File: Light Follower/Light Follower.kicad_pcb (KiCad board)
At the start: 2 copper layers, 144.8 x 86.5 mm, 14 parts, among them P1 Digital, P2 Analog, P3 CONN_01X01, P4 CONN_01X01, P5 CONN_01X01, P6 CONN_01X01

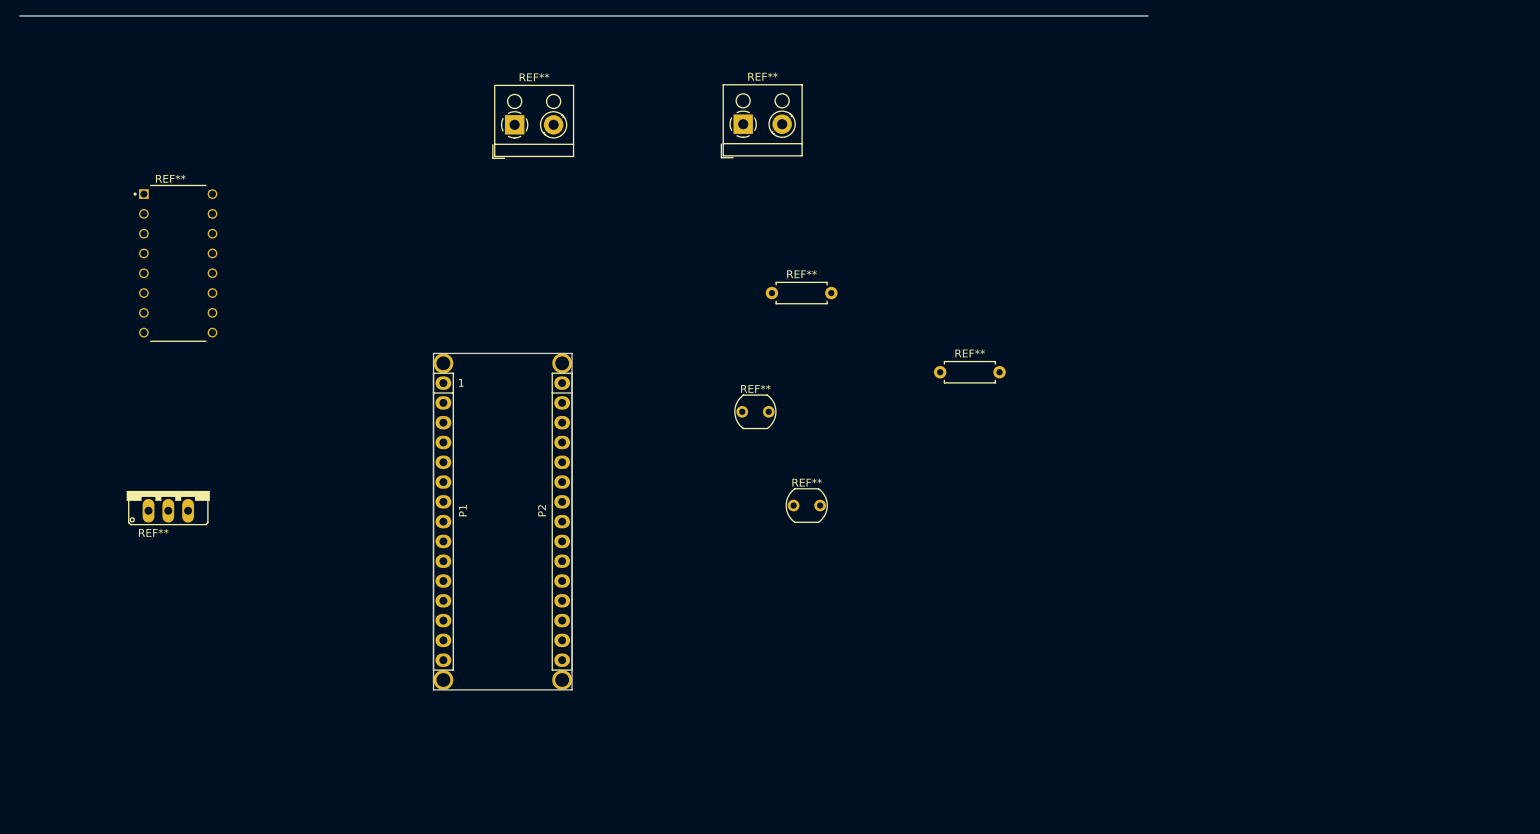
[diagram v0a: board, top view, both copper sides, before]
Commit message: Added PCB Design and LDR Modules
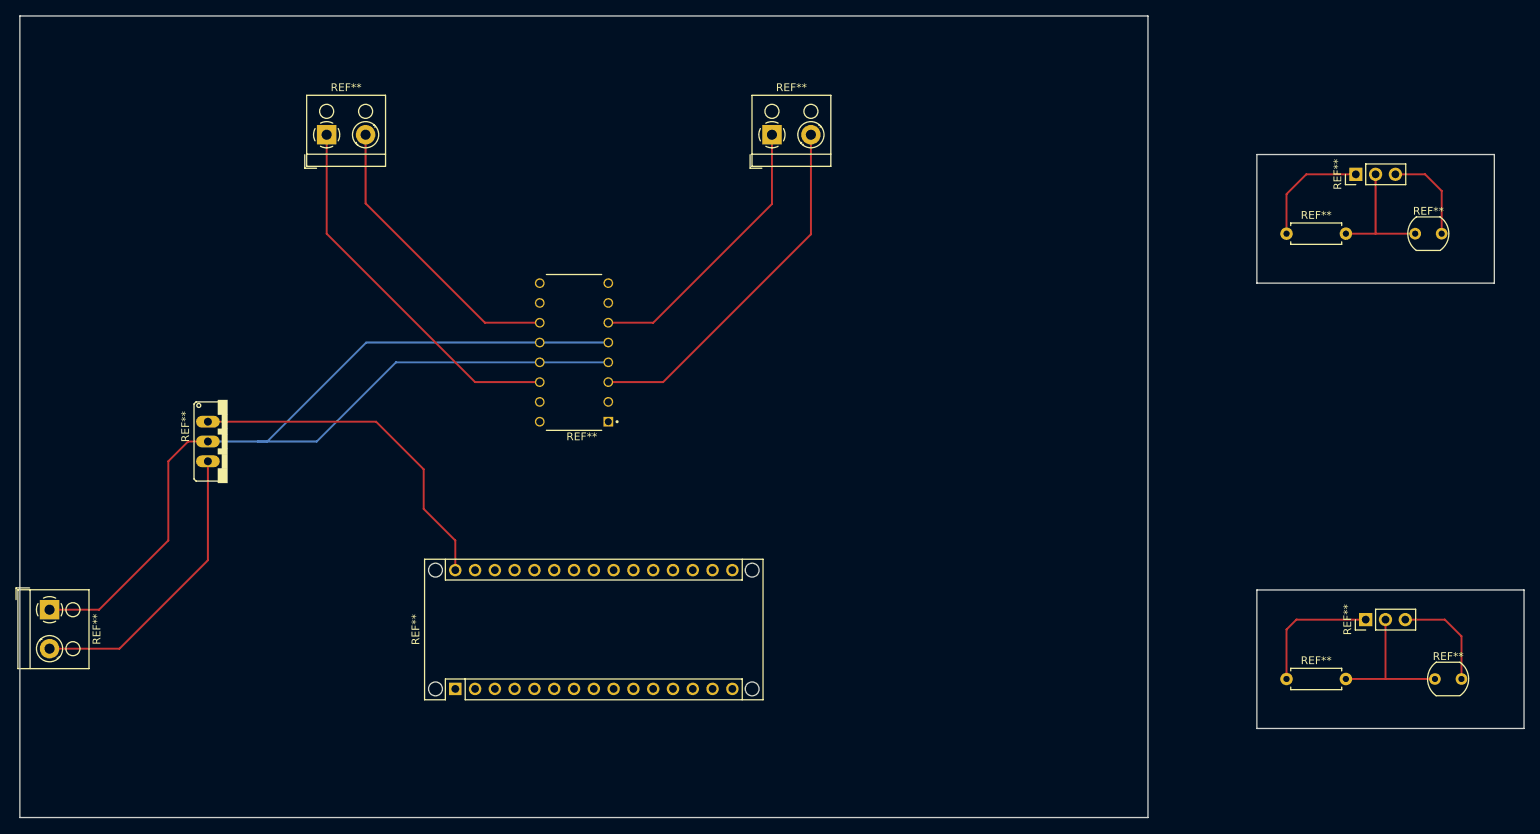
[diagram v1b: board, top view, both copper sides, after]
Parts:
- removed P1: Digital, Socket_Arduino_Nano:Socket_Strip_Arduino_1x15
- removed P2: Analog, Socket_Arduino_Nano:Socket_Strip_Arduino_1x15
- removed P3, P4, P5, P6: CONN_01X01, Socket_Arduino_Nano:1pin_Nano
- added REF**: Arduino_Nano_WithMountingHoles, Module:Arduino_Nano_WithMountingHoles, F.Cu at (141.0, 110.5)
- added REF**: PinHeader_1x03_P2.54mm_Vertical, Connector_PinHeader_2.54mm:PinHeader_1x03_P2.54mm_Vertical, F.Cu at (257.8, 101.6)
- added REF**: PinHeader_1x03_P2.54mm_Vertical, Connector_PinHeader_2.54mm:PinHeader_1x03_P2.54mm_Vertical, F.Cu at (256.5, 44.5)
- added REF**: TerminalBlock_RND_205-00001_1x02_P5.00mm_Horizontal, TerminalBlock_RND:TerminalBlock_RND_205-00001_1x02_P5.00mm_Horizontal, F.Cu at (88.9, 100.3)
- moved REF** 89.3 mm to (264.2, 52.1)
- moved REF** 85.3 mm to (266.7, 109.2)
- moved REF** 66.5 mm to (247.7, 52.1)
- moved REF** 59.4 mm to (247.7, 109.2)
- moved REF** 52.1 mm to (156.2, 67.3), turned to 180 degrees
- moved REF** 24.2 mm to (124.5, 39.4)
- moved REF** 9.92 mm to (111.8, 78.7), turned to 270 degrees
- moved REF** 3.93 mm to (181.6, 39.4)
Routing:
- net (no net): track 0.00 -> 485.5 mm
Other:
- board size 144.8 x 86.5 mm -> 193 x 102.9 mm
- board text removed: "1"
